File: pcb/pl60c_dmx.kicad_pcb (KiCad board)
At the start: 2 copper layers, 80 x 54 mm, 39 parts, among them J1 USB-C 16P, J2 XLR-5 female (DMX OUT), J3 DMX pigtail, J4 EXPANSION, J5 UART0, Q1 S8050, SW1 RESET, SW2 BOOT, SW3 USER, U1 ESP32-S3-WROOM-1-N16R8, U2 AMS1117-3.3, U3 SP3485EN, U4 USBLC6-2SC6

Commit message: auto: 2026-09-02 13:20:58
Co-Authored-By: Claude Fable 5.1 <noreply@anthropic.com>
Claude-Session: https://claude.ai/code/session_01WsrVZb94LwbHVAmBvsSTfn
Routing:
- net +3V3: track 177.8 -> 154.4 mm, vias 3 -> 2
- net GND: track 368.9 -> 390.3 mm
- net EN: track 55.8 -> 74.6 mm
- net CC2: track 10.3 -> 15.8 mm, vias 0 -> 2
- net USB_D-: track 27.6 -> 32.9 mm, vias 2 -> 3
- net DMX_TX: track 38.4 -> 43.1 mm
- net DMX_B: track 65.7 -> 61.6 mm
- net USB_D+: track 41.9 -> 44.7 mm, vias 4 -> 3
- net BUZZER: track 48.3 -> 50.0 mm
- net EXP_IO11: track 21.9 -> 23.5 mm
- net DMX_RX: track 36.3 -> 35.2 mm
- net BZ_N: track 15.8 -> 15.2 mm, vias 2 -> 0

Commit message: auto: 2026-09-02 13:23:01
Co-Authored-By: Claude Fable 5.1 <noreply@anthropic.com>
Claude-Session: https://claude.ai/code/session_01WsrVZb94LwbHVAmBvsSTfn
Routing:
- net GND: track 390.3 -> 478.4 mm
- net EN: track 74.6 -> 55.9 mm
- net DMX_TX: track 43.1 -> 26.8 mm
- net IO0_BOOT: track 48.4 -> 63.6 mm
- net +3V3: track 154.4 -> 148.5 mm, vias 2 -> 3
- net DMX_RX: track 35.2 -> 31.8 mm
- net CC2: track 15.8 -> 12.5 mm
- net DMX_B: track 61.6 -> 58.8 mm
- net +5V: track 89.6 -> 91.6 mm, vias 2 -> 0
- net USB_D+: track 44.7 -> 46.5 mm
- net BUZZER: track 50.0 -> 48.4 mm
- net DMX_A: track 55.4 -> 54.4 mm, vias 1 -> 0
- net VBUS: track 45.1 -> 44.5 mm
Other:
- board text added: "PL60C DMX wake-up rev A 2026-09"
- board text added: "github.com/tsmiltonAgents/pl60c-dmx-wakeup"

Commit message: auto: 2026-09-02 13:25:05
Co-Authored-By: Claude Fable 5.1 <noreply@anthropic.com>
Claude-Session: https://claude.ai/code/session_01WsrVZb94LwbHVAmBvsSTfn
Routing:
- net IO0_BOOT: track 63.6 -> 43.0 mm
- net DMX_TX: track 26.8 -> 45.7 mm
- net DMX_RX: track 31.8 -> 43.5 mm
- net +3V3: track 148.5 -> 158.8 mm, vias 3 -> 4
- net LED_DATA: track 29.5 -> 35.7 mm
- net DMX_B: track 58.8 -> 61.6 mm
- net GND: track 478.4 -> 480.5 mm
- net +5V: track 91.6 -> 89.5 mm, vias 0 -> 2
- net BUZZER: track 48.4 -> 46.8 mm
- net USB_D+: track 46.5 -> 44.9 mm
- net EN: track 55.9 -> 57.4 mm
- net DMX_DE: track 32.1 -> 31.0 mm
- net DMX_A: track 54.4 -> 55.4 mm, vias 0 -> 1

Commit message: auto: 2026-09-02 13:27:07
Co-Authored-By: Claude Fable 5.1 <noreply@anthropic.com>
Claude-Session: https://claude.ai/code/session_01WsrVZb94LwbHVAmBvsSTfn
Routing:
- net GND: track 480.5 -> 32.1 mm
- net +3V3: track 158.8 -> 0.00 mm, vias 4 -> 0
- net +5V: track 89.5 -> 0.00 mm, vias 2 -> 0
- net DMX_B: track 61.6 -> 0.00 mm, vias 2 -> 0
- net BTN_USER: track 59.1 -> 0.00 mm, vias 2 -> 0
- net EN: track 57.4 -> 0.00 mm, vias 2 -> 0
- net DMX_A: track 55.4 -> 0.00 mm, vias 1 -> 0
- net BUZZER: track 46.8 -> 0.00 mm, vias 2 -> 0
- net DMX_TX: track 45.7 -> 0.00 mm, vias 2 -> 0
- net DMX_RX: track 43.5 -> 0.00 mm, vias 2 -> 0
- net IO0_BOOT: track 43.0 -> 0.00 mm, vias 2 -> 0
- net LED_DATA: track 35.7 -> 0.00 mm, vias 2 -> 0
- net DMX_DE: track 31.0 -> 0.00 mm, vias 2 -> 0
- net USB_D+: track 44.9 -> 14.0 mm, vias 3 -> 2
- net VBUS: track 44.5 -> 15.7 mm, vias 3 -> 2
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
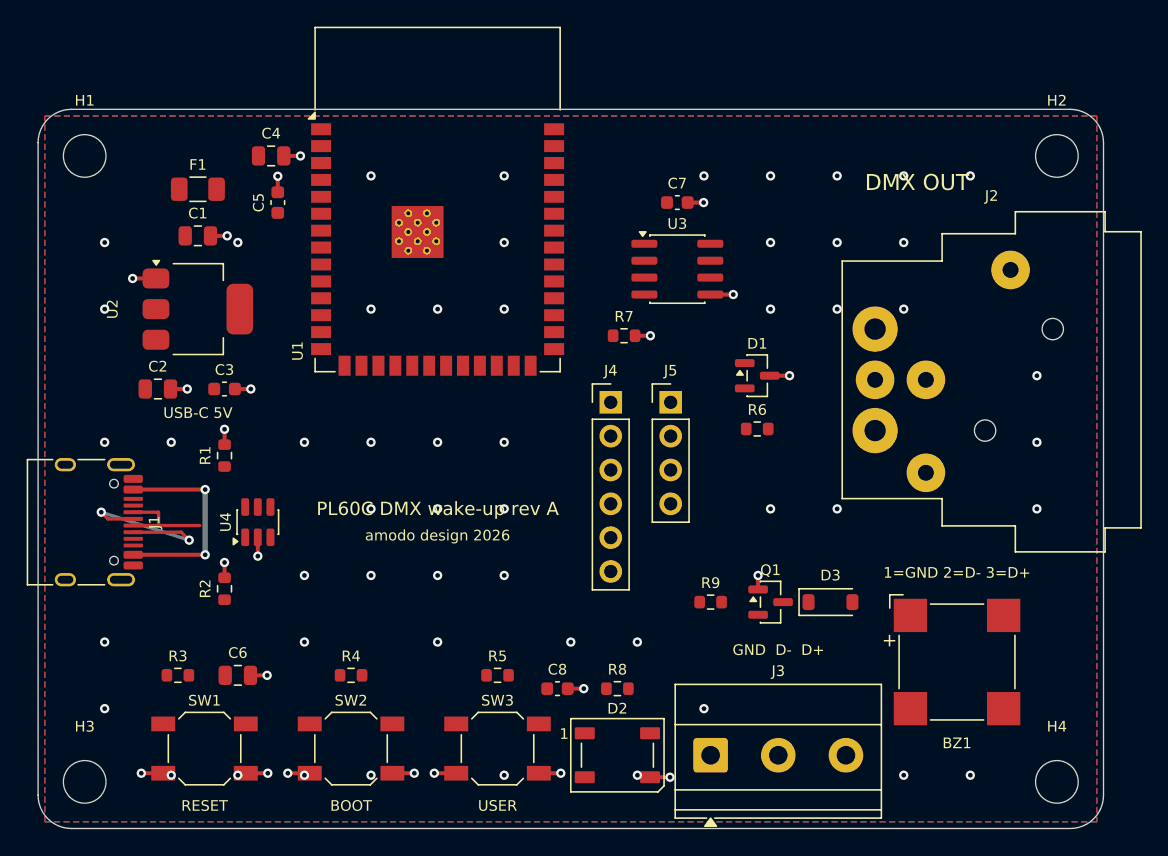
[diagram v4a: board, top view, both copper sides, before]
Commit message: PL60C DMX wake-up controller rev A: verified design, JLCPCB production files, docs
- ESP32-S3-WROOM-1 + SP3485EN DMX512 transmitter, XLR-5 out, USB-C power
- generated schematic/PCB (KiCad 10), Freerouting autoroute, ERC/DRC clean
- Gerbers, JLCPCB BOM + CPL, LCSC stock-verified parts, README + pin map

Co-Authored-By: Claude Fable 5.1 <noreply@anthropic.com>
Claude-Session: https://claude.ai/code/session_01WsrVZb94LwbHVAmBvsSTfn
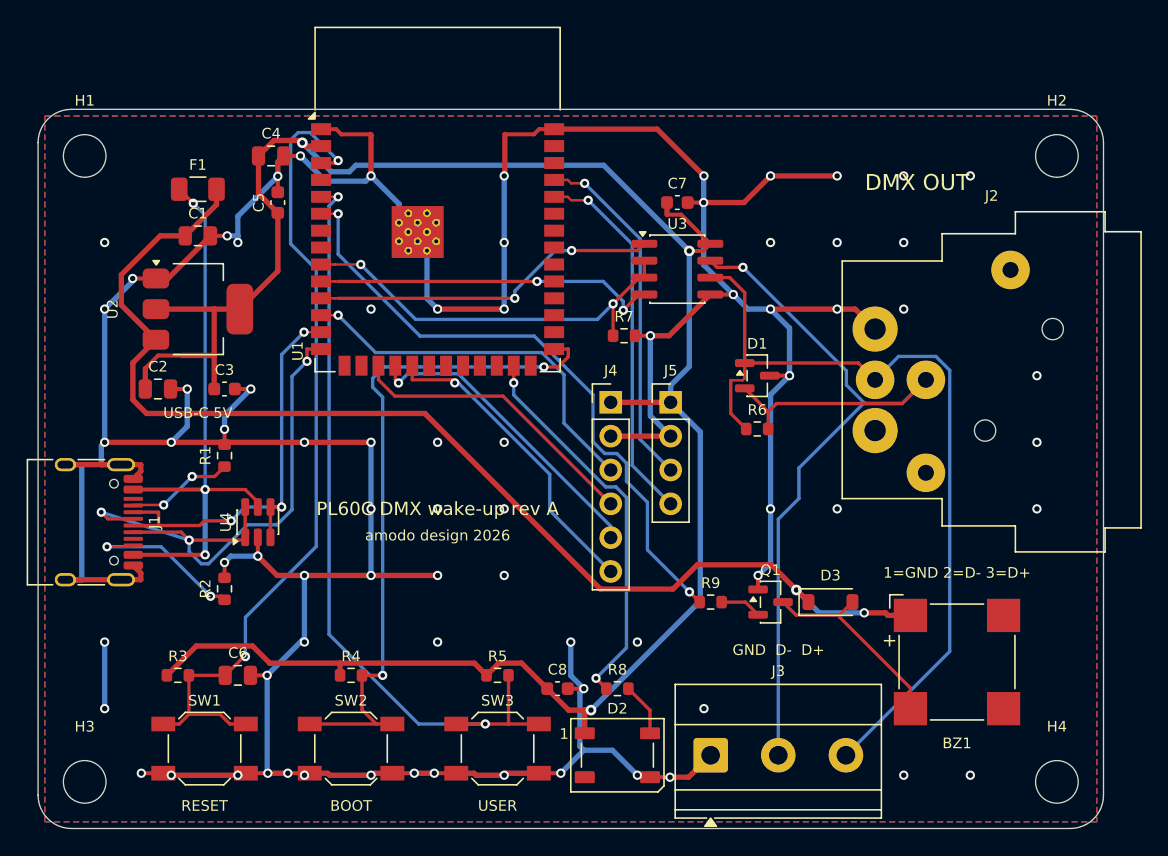
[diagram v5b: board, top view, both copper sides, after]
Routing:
- net GND: track 32.1 -> 347.5 mm
- net +3V3: track 0.00 -> 159.8 mm, vias 0 -> 3
- net +5V: track 0.00 -> 89.6 mm, vias 0 -> 2
- net DMX_B: track 0.00 -> 67.7 mm, vias 0 -> 1
- net DMX_A: track 0.00 -> 63.9 mm
- net EN: track 0.00 -> 62.4 mm, vias 0 -> 2
- net BTN_USER: track 0.00 -> 58.8 mm, vias 0 -> 2
- net IO0_BOOT: track 0.00 -> 51.4 mm, vias 0 -> 2
- net BUZZER: track 0.00 -> 47.2 mm, vias 0 -> 2
- net DMX_DE: track 0.00 -> 31.0 mm, vias 0 -> 2
- net USB_D+: track 14.0 -> 44.8 mm, vias 2 -> 3
- net LED_DATA: track 0.00 -> 29.5 mm, vias 0 -> 2
- net EXP_SDA: track 0.00 -> 28.7 mm, vias 0 -> 1
- net VBUS: track 15.7 -> 43.8 mm, vias 2 -> 3
- net RXD0: track 0.00 -> 28.0 mm, vias 0 -> 1
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
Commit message: auto: 2026-09-02 13:40:12
Co-Authored-By: Claude Fable 5.1 <noreply@anthropic.com>
Claude-Session: https://claude.ai/code/session_01WsrVZb94LwbHVAmBvsSTfn
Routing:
- net GND: track 347.5 -> 395.7 mm
- net DMX_TX: track 26.1 -> 43.4 mm
- net +3V3: track 159.8 -> 174.0 mm
- net DMX_RX: track 26.3 -> 39.6 mm
- net DMX_A: track 63.9 -> 55.4 mm, vias 0 -> 1
- net +5V: track 89.6 -> 98.1 mm
- net DMX_B: track 67.7 -> 61.6 mm, vias 1 -> 2
- net IO0_BOOT: track 51.4 -> 57.1 mm
- net EN: track 62.4 -> 66.9 mm
- net BTN_USER: track 58.8 -> 55.8 mm
- net LED_DATA: track 29.5 -> 27.5 mm
- net EXP_IO11: track 23.5 -> 25.4 mm
- net EXP_SCL: track 22.4 -> 24.1 mm, vias 0 -> 1
- net EXP_SDA: track 28.7 -> 27.0 mm
- net EXP_IO10: track 23.2 -> 24.7 mm
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
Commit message: auto: 2026-09-02 14:26:12
Co-Authored-By: Claude Fable 5.1 <noreply@anthropic.com>
Claude-Session: https://claude.ai/code/session_01WsrVZb94LwbHVAmBvsSTfn
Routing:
- net GND: track 395.7 -> 472.7 mm
- net DMX_TX: track 43.4 -> 27.7 mm
- net DMX_RX: track 39.6 -> 26.0 mm
- net +5V: track 98.1 -> 86.0 mm, vias 2 -> 4
- net +3V3: track 174.0 -> 166.7 mm, vias 3 -> 4
- net IO0_BOOT: track 57.1 -> 64.2 mm
- net USB_D+: track 44.7 -> 38.5 mm, vias 3 -> 4
- net EN: track 66.9 -> 62.0 mm
- net BUZZER: track 47.3 -> 51.6 mm
- net CC2: track 12.5 -> 9.05 mm
- net VBUS: track 44.5 -> 47.8 mm, vias 3 -> 4
- net RXD0: track 27.4 -> 30.3 mm
- net TXD0: track 26.2 -> 28.6 mm
- net DMX_B: track 61.6 -> 60.5 mm
- net DMX_A: track 55.4 -> 54.6 mm
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
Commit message: auto: 2026-09-02 14:48:00
Co-Authored-By: Claude Fable 5.1 <noreply@anthropic.com>
Claude-Session: https://claude.ai/code/session_01WsrVZb94LwbHVAmBvsSTfn
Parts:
- added R10: 10R, R_1206_3216Metric, F.Cu at (52.0, 40.5)
- C2: value 10uF -> 22uF
- D2: value WS2812B -> WS2812B-2020; footprint LED_WS2812B_PLCC4_5.0x5.0mm_P3.2mm -> LED_WS2812B-2020_PLCC4_2.0x2.0mm
- R9: value 1k -> 470R
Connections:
- BZ1 pad 1: +5V -> BZ_P
- D2 pad 1: +3V3 -> (no net)
- D2 pad 2: (no net) -> GND
- D2 pad 3: GND -> LED_DATA_R
- D2 pad 4: LED_DATA_R -> +3V3
- D3 pad 1: +5V -> BZ_P
- Q1 pad 1: GND -> Q1_B
- Q1 pad 2: Q1_B -> GND
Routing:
- net BZ_P: track 0.00 -> 22.8 mm
- net IO0_BOOT: track 64.2 -> 47.5 mm, vias 2 -> 4
- net +5V: track 86.0 -> 71.5 mm
- net GND: track 472.7 -> 465.8 mm
- net BUZZER: track 51.6 -> 45.4 mm
- net EXP_IO10: track 25.2 -> 31.2 mm
- net DMX_RX: track 26.0 -> 31.7 mm
- net USB_D-: track 32.7 -> 37.5 mm
- net USB_D+: track 38.5 -> 42.1 mm
- net EXP_SDA: track 27.1 -> 30.1 mm
- net LED_DATA: track 27.4 -> 30.1 mm, vias 2 -> 0
- net LED_DATA_R: track 4.02 -> 6.62 mm
- net EXP_IO11: track 26.1 -> 28.6 mm
- net EXP_SCL: track 24.6 -> 22.4 mm, vias 1 -> 0
- net EN: track 62.0 -> 63.9 mm
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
